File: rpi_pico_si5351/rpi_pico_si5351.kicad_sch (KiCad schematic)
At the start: 15 parts, among them U1 Pico

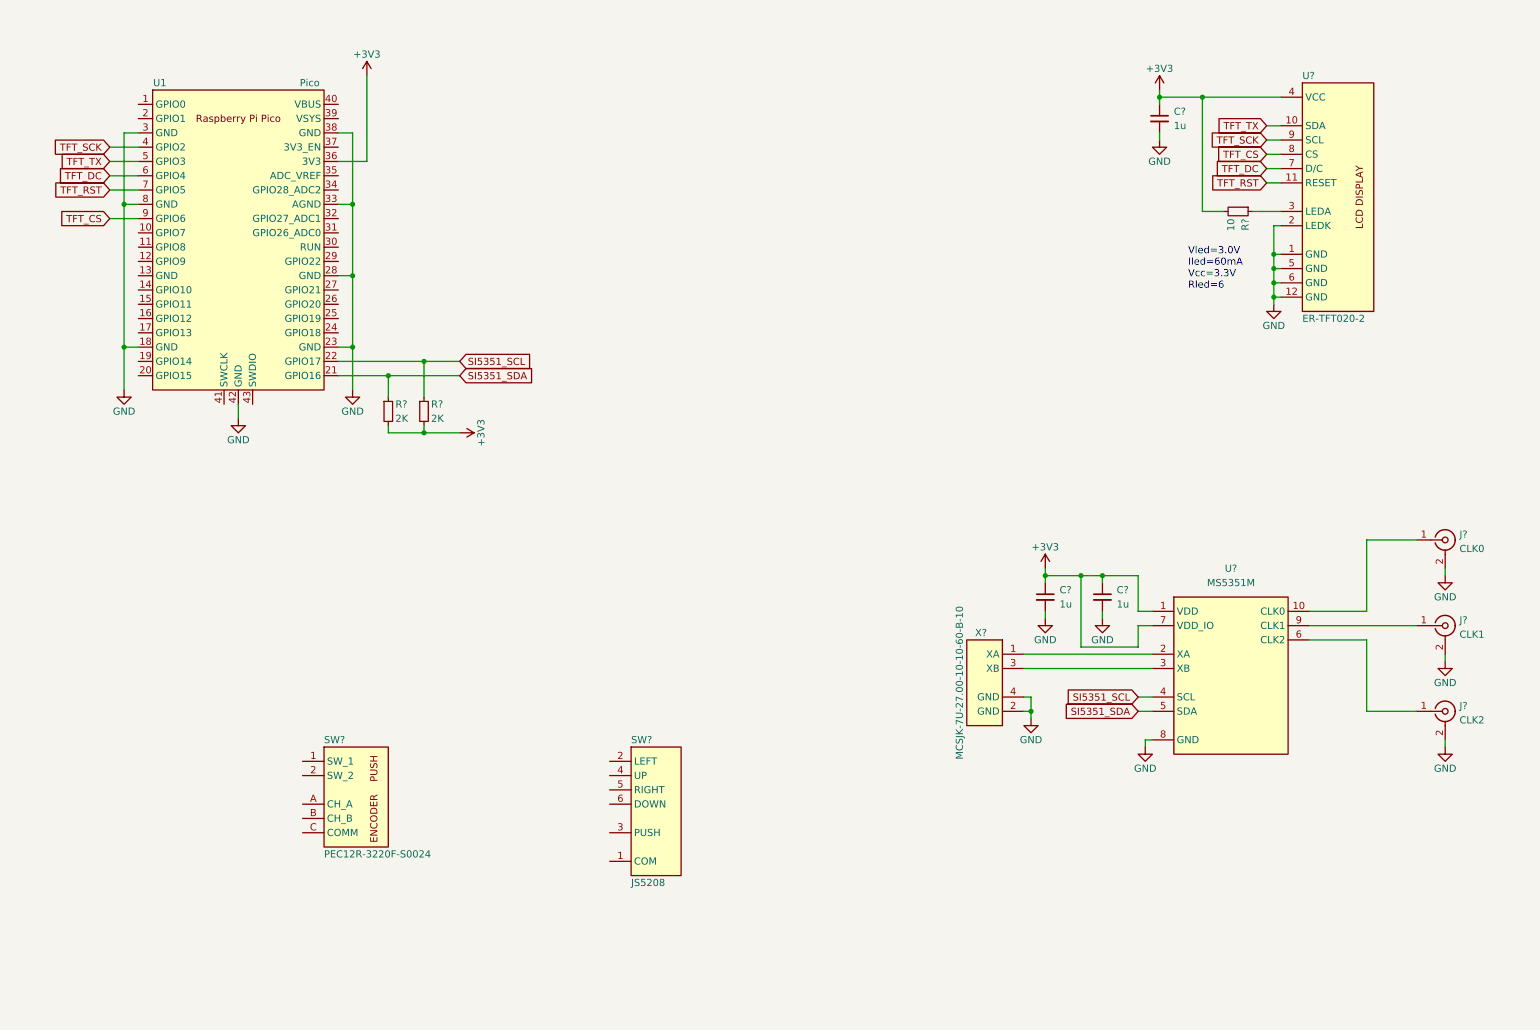
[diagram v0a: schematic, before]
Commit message: add LCD datasheet
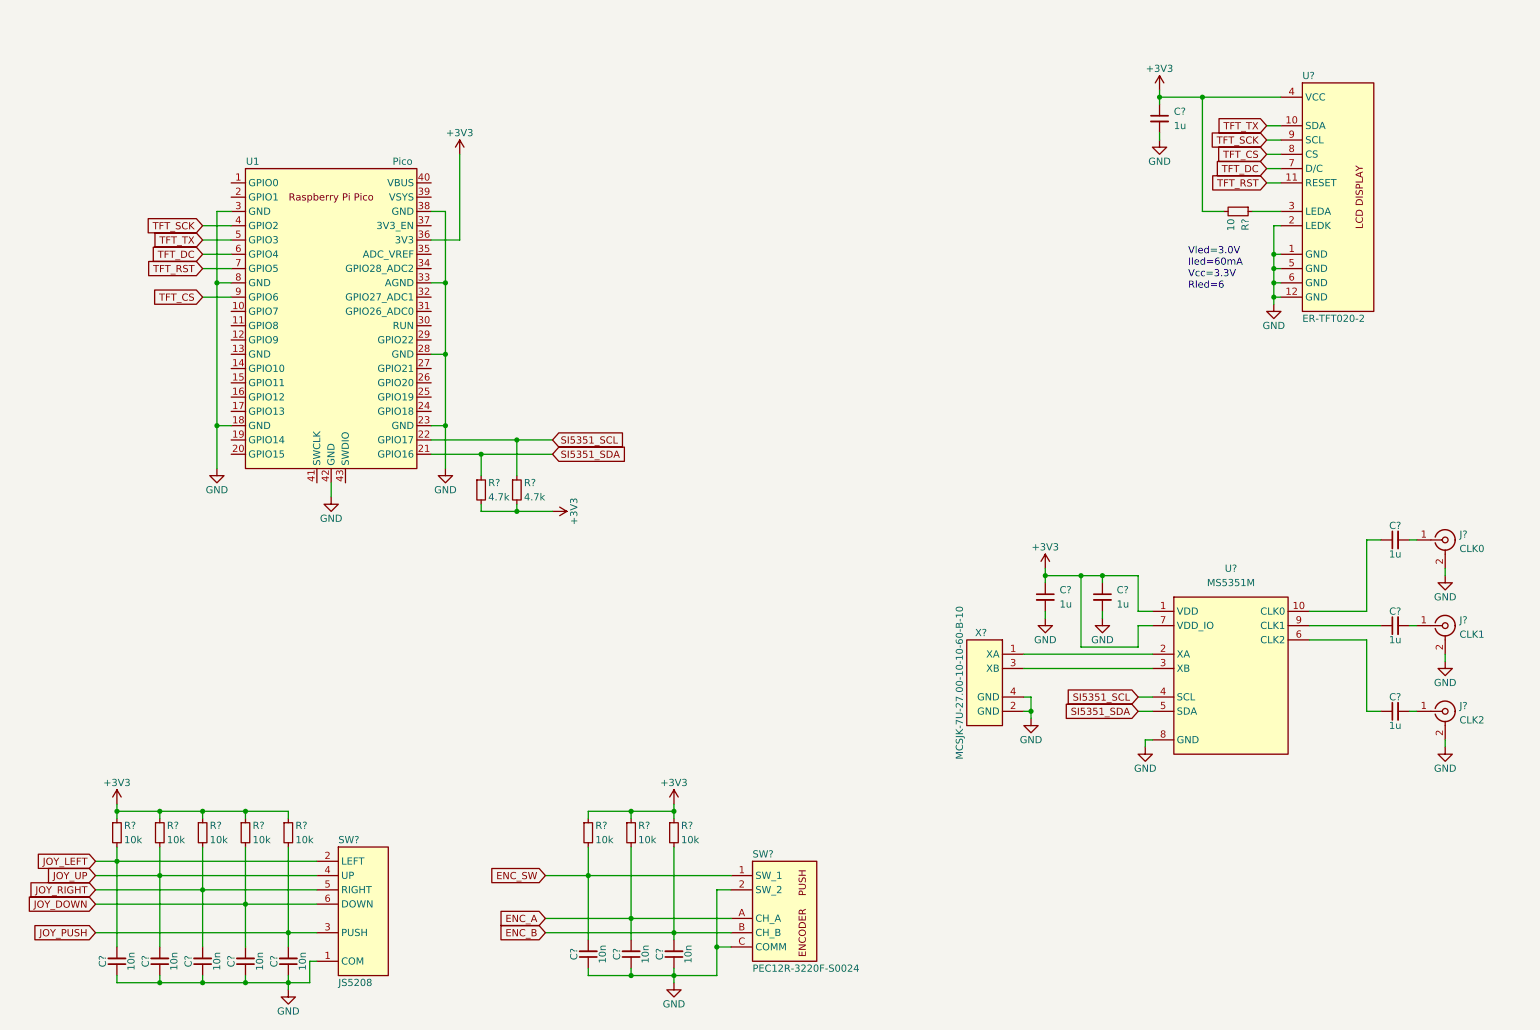
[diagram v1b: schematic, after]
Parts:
- added C? (x3): 1u, Capacitor_SMD:C_0805_2012Metric, symbol Device:C_Small
- added C? (x8): 10n, Capacitor_SMD:C_0805_2012Metric, symbol Device:C_Small
- added R? (x8): 10k, Resistor_SMD:R_0805_2012Metric, symbol Device:R_Small
- R? (x2): value 2K -> 4.7k
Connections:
- net +3V3: now also R?.1, R?.1, R?.1, R?.1, R?.1, R?.1, R?.1, R?.1
- net GND: now also SW?.1 (COM), SW?.2 (SW_2), SW?.C (COMM), C?.1, C?.1, C?.1, C?.1, C?.1, C?.1, C?.1, C?.1
- net at U?.10 (CLK0): now also C?.1; no longer J?.1 (In)
- net at U?.6 (CLK2): now also C?.1; no longer J?.1 (In)
- net at U?.9 (CLK1): now also C?.1; no longer J?.1 (In)
- net ENC_SW: now reaches SW?.1 (SW_1)
- net ENC_SW: now also C?.2, R?.2
- net ENC_A: now reaches SW?.A (CH_A)
- net ENC_A: now also C?.2, R?.2
- net ENC_B: now reaches SW?.B (CH_B)
- net ENC_B: now also C?.2, R?.2
- net JOY_LEFT: now reaches SW?.2 (LEFT)
- net JOY_LEFT: now also C?.2, R?.2
- net JOY_PUSH: now reaches SW?.3 (PUSH)
- net JOY_PUSH: now also C?.2, R?.2
- net JOY_UP: now reaches SW?.4 (UP)
- net JOY_UP: now also C?.2, R?.2
- net JOY_RIGHT: now reaches SW?.5 (RIGHT)
- net JOY_RIGHT: now also C?.2, R?.2
- net JOY_DOWN: now reaches SW?.6 (DOWN)
- net JOY_DOWN: now also C?.2, R?.2
- new net: C?.2, J?.1 (In) (x3)
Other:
- moved on the sheet: R?, SW?, U1

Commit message: initial board layout
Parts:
- added H1, H2, H3, H4: M3, MountingHole:MountingHole_3.2mm_M3_DIN965_Pad_TopBottom, symbol Mechanical:MountingHole
- J1, J2, J3: renamed from J?; footprint (none) -> parts:SMA
- SW1: renamed from SW?; footprint (none) -> parts:JS_5208
- SW2: renamed from SW?; footprint (none) -> parts:PEC12R-3220F-S0024
- U1: renamed from U?; footprint (none) -> parts:ER-TFT020-2
- U2: renamed from U1; footprint RPi_Pico:RPi_Pico_SMD_TH -> MCU_RaspberryPi_and_Boards:RPi_Pico_SMD_TH
- gave numbers to parts that had none: 27

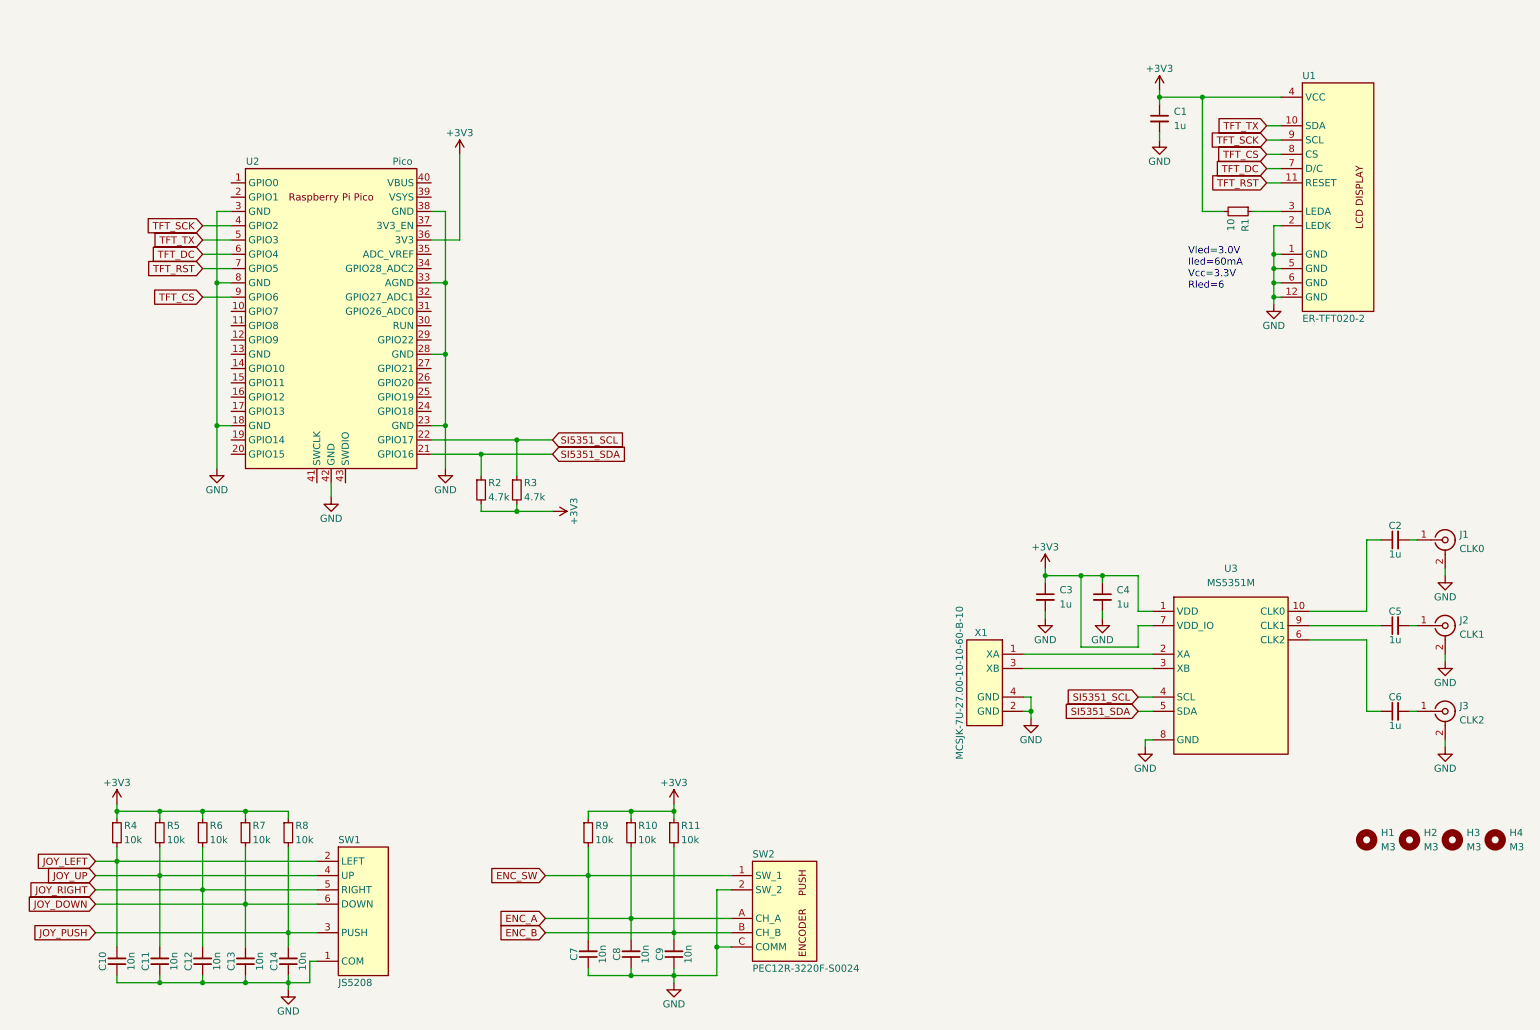
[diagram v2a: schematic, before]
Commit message: fix footprints, update schematic
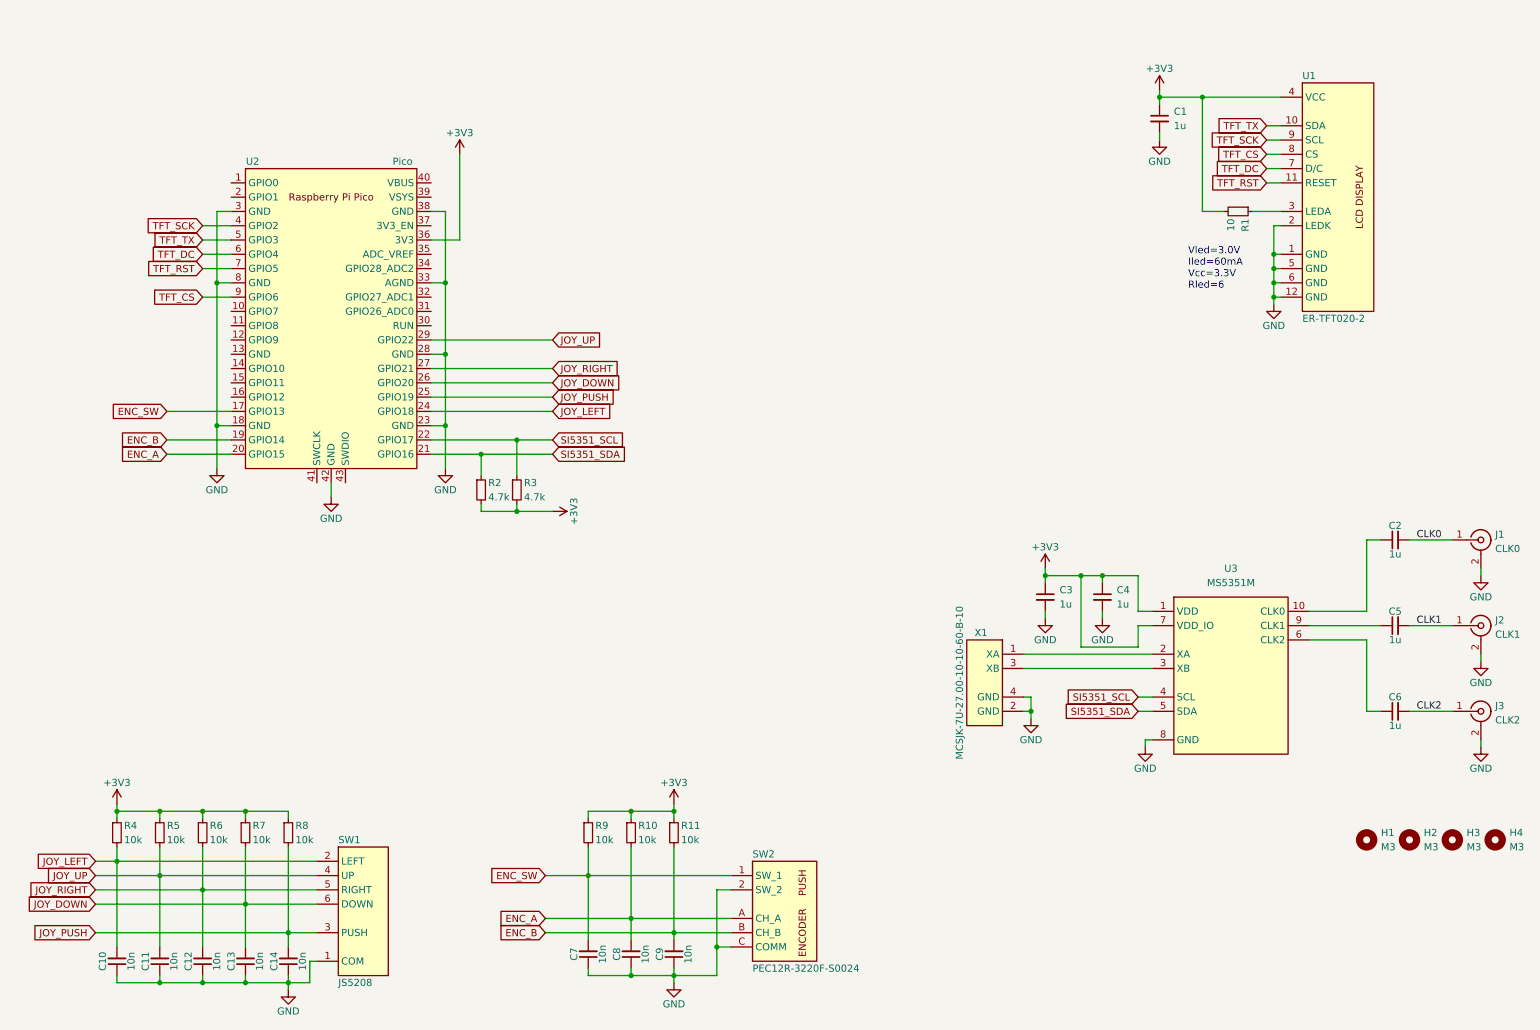
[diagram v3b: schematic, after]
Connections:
- net ENC_A: now also U2.20 (GPIO15)
- net ENC_B: now also U2.19 (GPIO14)
- net ENC_SW: now also U2.17 (GPIO13)
- net JOY_DOWN: now also U2.26 (GPIO20)
- net JOY_LEFT: now also U2.24 (GPIO18)
- net JOY_PUSH: now also U2.25 (GPIO19)
- net JOY_RIGHT: now also U2.27 (GPIO21)
- net JOY_UP: now also U2.29 (GPIO22)
- net CLK0: now reaches C2.2, J1.1 (In)
- net CLK2: now reaches C6.2, J3.1 (In)
- net CLK1: now reaches C5.2, J2.1 (In)
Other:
- moved on the sheet: J1, J2, J3

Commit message: add multi-board header to allow stacking of multiple modules
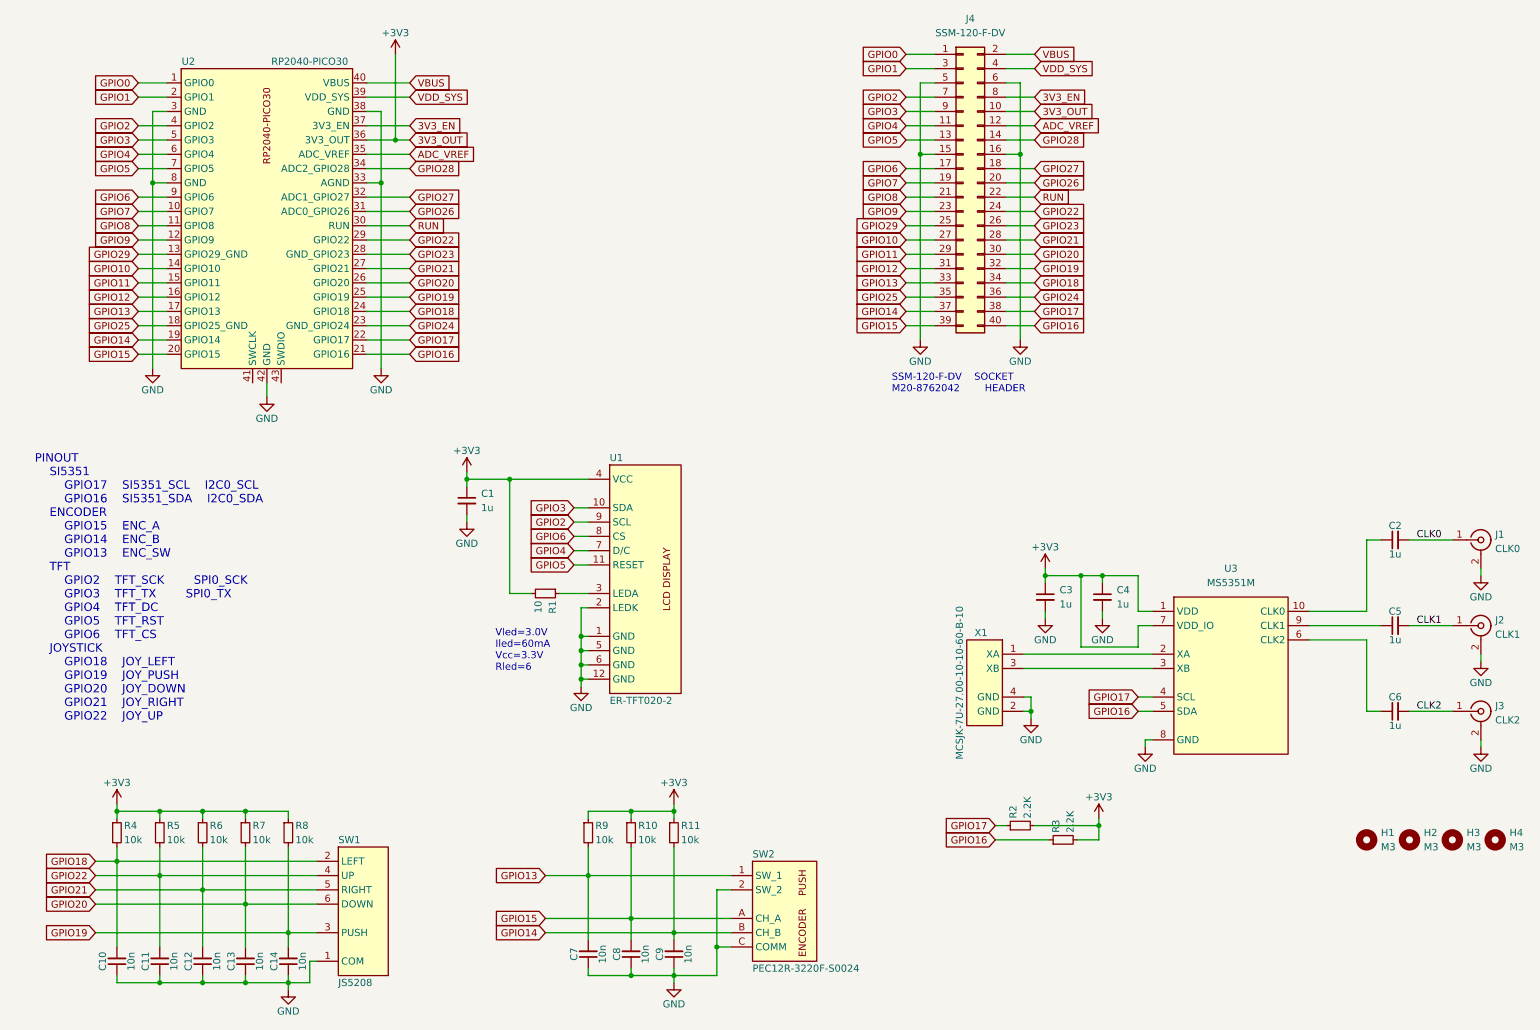
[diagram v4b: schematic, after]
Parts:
- removed U2: Pico, MCU_RaspberryPi_and_Boards:RPi_Pico_SMD_TH, symbol MCU_RaspberryPi_and_Boards:Pico
- added J4: SSM-120-F-DV, Connector_PinSocket_2.54mm:PinSocket_2x20_P2.54mm_Vertical_SMD, symbol Connector_Generic:Conn_02x20_Odd_Even
- added U2: RP2040-PICO30, parts:RP2040_PICO30_SMD, symbol parts:RP2040-PICO30
- R2, R3: value 4.7k -> 2.2K
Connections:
- net +3V3: now also J4.10 (Pin_10), U2.36 (3V3_OUT)
- net GND: now also J4.15 (Pin_15), J4.16 (Pin_16), J4.5 (Pin_5), J4.6 (Pin_6), U2.3 (GND), U2.33 (AGND), U2.38 (GND), U2.42 (GND), U2.8 (GND)
- net ENC_A renamed GPIO15
- net GPIO15: now also J4.39 (Pin_39), U2.20 (GPIO15)
- net ENC_B renamed GPIO14
- net GPIO14: now also J4.37 (Pin_37), U2.19 (GPIO14)
- net ENC_SW renamed GPIO13
- net GPIO13: now also J4.33 (Pin_33), U2.17 (GPIO13)
- net JOY_DOWN renamed GPIO20
- net GPIO20: now also J4.30 (Pin_30), U2.26 (GPIO20)
- net JOY_LEFT renamed GPIO18
- net GPIO18: now also J4.34 (Pin_34), U2.24 (GPIO18)
- net JOY_PUSH renamed GPIO19
- net GPIO19: now also J4.32 (Pin_32), U2.25 (GPIO19)
- net JOY_RIGHT renamed GPIO21
- net GPIO21: now also J4.28 (Pin_28), U2.27 (GPIO21)
- net JOY_UP renamed GPIO22
- net GPIO22: now also J4.24 (Pin_24), U2.29 (GPIO22)
- net SI5351_SCL renamed GPIO16
- net GPIO16: now also U3.5 (SDA), J4.40 (Pin_40), U2.21 (GPIO16); no longer U3.4 (SCL)
- net SI5351_SDA renamed GPIO17
- net GPIO17: now also U3.4 (SCL), J4.38 (Pin_38), U2.22 (GPIO17); no longer U3.5 (SDA)
- net TFT_CS renamed GPIO6
- net GPIO6: now also J4.17 (Pin_17), U2.9 (GPIO6)
- net TFT_DC renamed GPIO4
- net GPIO4: now also J4.11 (Pin_11), U2.6 (GPIO4)
- net TFT_RST renamed GPIO5
- net GPIO5: now also J4.13 (Pin_13), U2.7 (GPIO5)
- net TFT_SCK renamed GPIO2
- net GPIO2: now also J4.7 (Pin_7), U2.4 (GPIO2)
- net TFT_TX renamed GPIO3
- net GPIO3: now also J4.9 (Pin_9), U2.5 (GPIO3)
- new net 3V3_EN: J4.8 (Pin_8), U2.37 (3V3_EN)
- new net ADC_VREF: J4.12 (Pin_12), U2.35 (ADC_VREF)
- new net GPIO0: J4.1 (Pin_1), U2.1 (GPIO0)
- new net GPIO1: J4.3 (Pin_3), U2.2 (GPIO1)
- new net GPIO10: J4.27 (Pin_27), U2.14 (GPIO10)
- new net GPIO11: J4.29 (Pin_29), U2.15 (GPIO11)
- new net GPIO12: J4.31 (Pin_31), U2.16 (GPIO12)
- new net GPIO23: J4.26 (Pin_26), U2.28 (GND_GPIO23)
- new net GPIO24: J4.36 (Pin_36), U2.23 (GND_GPIO24)
- new net GPIO25: J4.35 (Pin_35), U2.18 (GPIO25_GND)
- new net GPIO26: J4.20 (Pin_20), U2.31 (ADC0_GPIO26)
- new net GPIO27: J4.18 (Pin_18), U2.32 (ADC1_GPIO27)
- new net GPIO28: J4.14 (Pin_14), U2.34 (ADC2_GPIO28)
- new net GPIO29: J4.25 (Pin_25), U2.13 (GPIO29_GND)
- new net GPIO7: J4.19 (Pin_19), U2.10 (GPIO7)
- new net GPIO8: J4.21 (Pin_21), U2.11 (GPIO8)
- new net GPIO9: J4.23 (Pin_23), U2.12 (GPIO9)
- new net RUN: J4.22 (Pin_22), U2.30 (RUN)
- new net VBUS: J4.2 (Pin_2), U2.40 (VBUS)
- new net VDD_SYS: J4.4 (Pin_4), U2.39 (VDD_SYS)
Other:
- note added: "PINOUT SI5351 GPIO17 SI5351_SCL I2C0_SCL GPIO16 SI5351_SDA I2C0_SDA ENCODER GPIO15 ENC_A GPIO14 ENC_B GPIO13 ENC_SW TFT GPIO2 TFT_SCK SPI0_SCK GPIO3 TFT_TX SPI0_TX GPIO4 TFT_DC GPIO5 TFT_RST GPIO6 TFT_CS JOYSTICK GPIO18 JOY_LEFT GPIO19 JOY_PUSH GPIO20 JOY_DOWN GPIO21 JOY_RIGHT GPIO22 JOY_UP"
- note added: "SSM-120-F-DV SOCKET M20-8762042 HEADER"
- moved on the sheet: C1, R1, U1
